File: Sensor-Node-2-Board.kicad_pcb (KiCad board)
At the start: 2 copper layers, 100 x 100 mm, 67 parts, among them J401 EBWA-02-B, J701 PS0519, J702 EBWA-02-B, Q101 BC549, Q401 Si4944DY, SW501 SW_HELP, U201 LM393, U601 Photon 2, U701 L7805

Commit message: feat: release
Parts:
- moved C701 12.6 mm to (203.0, 168.7)
- moved D702 12.6 mm to (192.5, 168.7)
- moved C101 12.6 mm to (260.0, 125.0)
- moved C102 12.6 mm to (232.5, 140.0)
- moved C103 12.6 mm to (248.8, 115.0)
- moved C201 12.6 mm to (250.0, 90.0)
- moved C202 12.6 mm to (231.3, 93.8)
- moved C301 12.6 mm to (218.7, 125.0)
- moved C401 12.6 mm to (180.0, 127.5)
- moved C402 12.6 mm to (185.0, 131.2)
- moved C501 12.6 mm to (181.2, 111.2)
- moved C502 12.6 mm to (205.0, 125.0)
- moved D101 12.6 mm to (252.5, 120.0)
- moved D401 12.6 mm to (180.0, 131.2)
- moved D501 12.6 mm to (175.0, 100.0)
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
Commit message: Update Outputs (release)
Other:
- board text added: "0.02mm"
- board text added: "0.035mm (1.00oz)"
- board text added: "1.49mm"
- board text added: "B.Mask"
- board text added: "B.Paste"
- board text added: "B.Silkscreen"
- board text added: "Copper"
- board text added: "Core"
- board text added: "Dielectric"
- board text added: "Direct Printing"
- board text added: "F.Mask"
- board text added: "F.Paste"
- board text added: "F.Silkscreen"
- board text added: "FR4_7628"
- board text added: "GBR"
- board text added: "Gerber"
- board text added: "L1 (Sig, PWR)"
- board text added: "L2 (Sig, GND)"
- board text added: "Layer"
- board text added: "Legend"
- board text added: "Material"
- board text added: "Note: external layer thicknesses are specified after plating"
- board text added: "Paste Mask"
- board text added: "Signal"
- board text added: "Solder Mask"
- board text added: "Solder Resist"
- board text added: "Thickness"
- board text added: "Total thickness: 1.6mm"
- board text added: "Type"

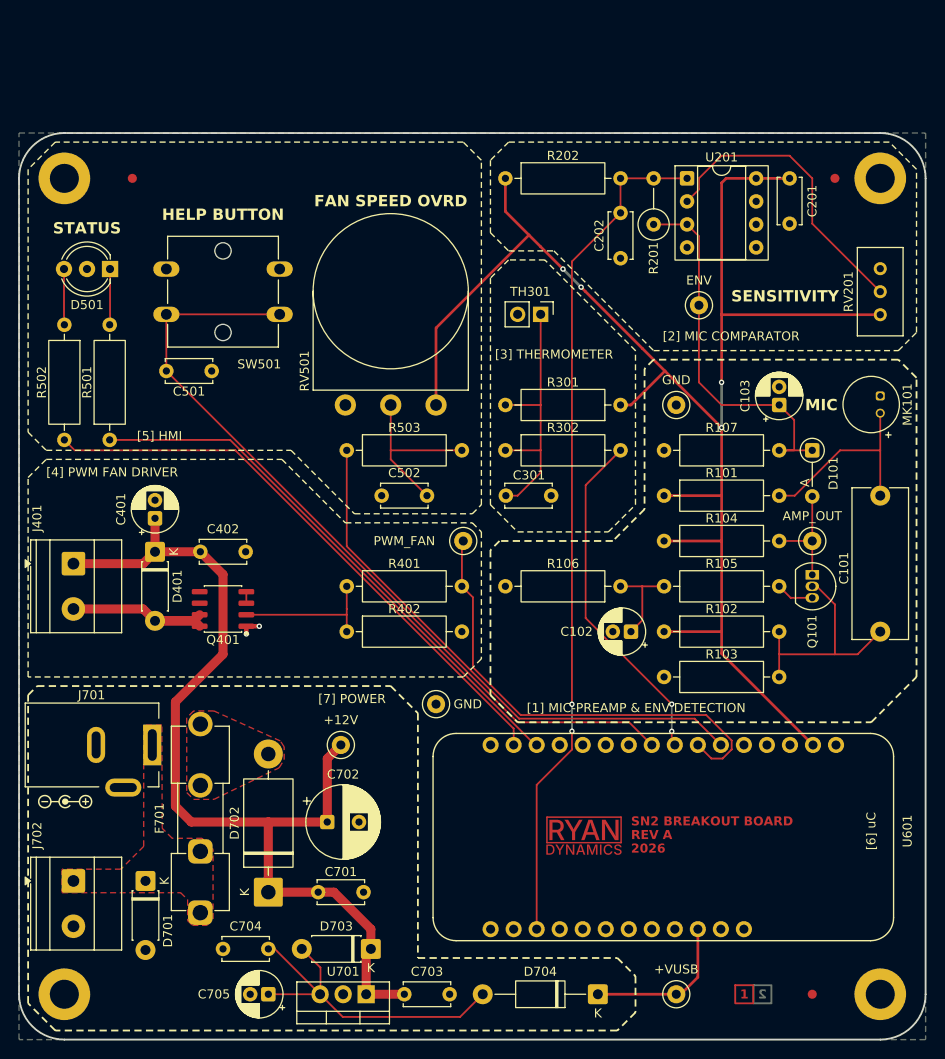
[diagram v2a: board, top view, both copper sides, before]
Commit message: fix: change status led wiring and improve 12V input protection
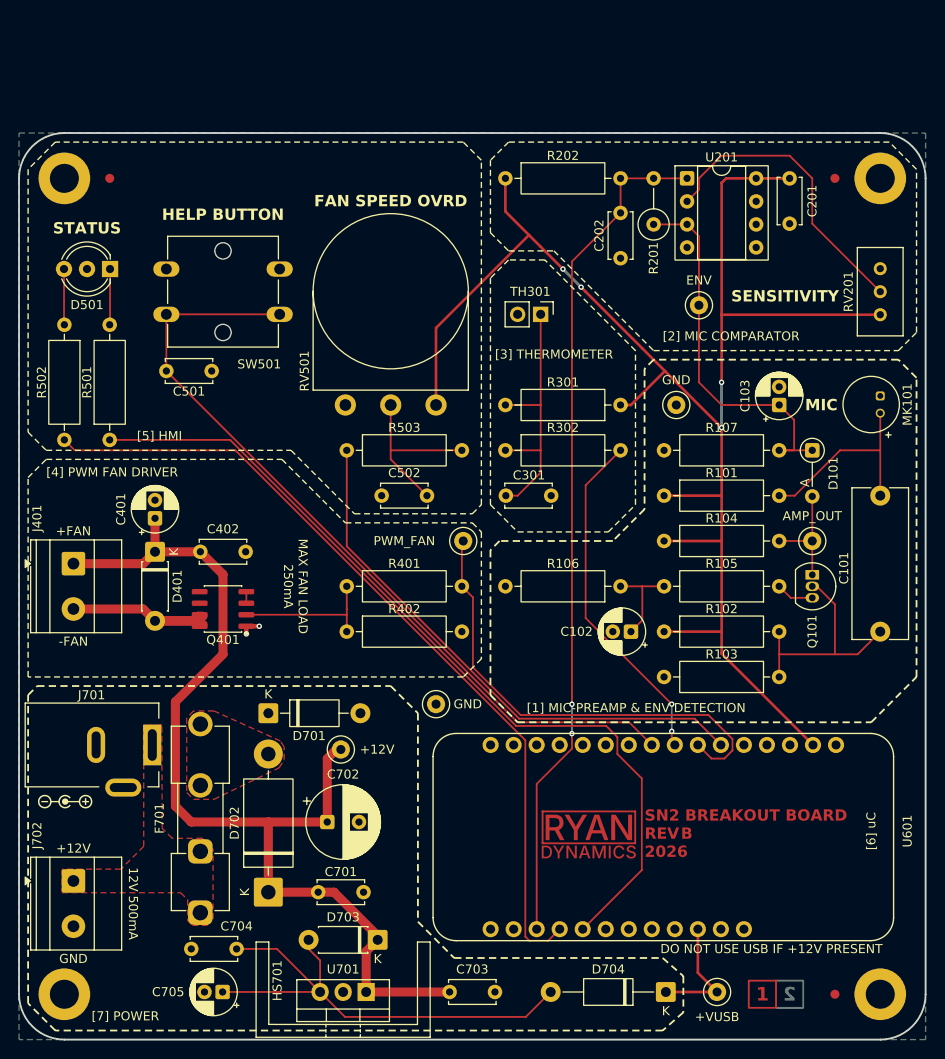
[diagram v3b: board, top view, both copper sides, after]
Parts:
- added HS701: Heatsink, RD-Heatsinks:Heatsink_6073B_19x9.5mm, F.Cu at (200.8, 184.6)
- D701: value P4KE16AC -> P4KE16; footprint Diode_THT:D_DO-41_SOD81_P7.62mm_Horizontal -> Diode_THT:D_DO-41_SOD81_P10.16mm_Horizontal
- F701: value 1A M205 -> 500mA M205
- ID901: footprint RD-Symbols-Silkscreen:STACKUP_ID_2L_SML -> RD-Symbols-Silkscreen:STACKUP_ID_2L
- moved D701 22.9 mm to (192.5, 149.0), turned to 0 degrees
- moved D704 7.50 mm to (236.3, 179.8)
- moved C705 5.05 mm to (187.5, 179.8)
- moved C703 5.01 mm to (217.5, 179.8)
- moved TP701 4.51 mm to (242.0, 179.8)
- moved C704 3.50 mm to (184.0, 175.0)
- moved FID901 2.50 mm to (175.0, 90.0)
- moved FID903 2.50 mm to (255.0, 180.0)
- moved ID901 2.50 mm to (248.5, 180.0)
- moved D703 1.25 mm to (204.6, 174.0)
- moved TP702 0.50 mm to (200.5, 153.0)
- moved U701 0.25 mm to (203.3, 179.8)
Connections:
- D701 pad 1: /SCHEMATIC/+12V_IN -> /SCHEMATIC/+12V_FUSED
- U601 pad 14: /SCHEMATIC/LED_RED -> unconnected-(U601-RX-Pad14)
- U601 pad 15: /SCHEMATIC/LED_GRN -> unconnected-(U601-TX-Pad15)
- U601 pad 20: unconnected-(U601-D3-Pad20) -> /SCHEMATIC/LED_GRN
- U601 pad 21: unconnected-(U601-D4-Pad21) -> /SCHEMATIC/LED_RED
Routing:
- net /SCHEMATIC/LED_RED: track 61.0 -> 94.6 mm
- net /SCHEMATIC/LED_GRN: track 64.6 -> 90.7 mm
- net /SCHEMATIC/+5V: track 39.4 -> 55.1 mm
- net +12V: track 108.5 -> 113.8 mm
- net +VUSB: track 17.1 -> 13.6 mm
- net /SCHEMATIC/FAN-: track 19.9 -> 20.5 mm
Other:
- board text added: "+12V"
- board text added: "+FAN"
- board text added: "-FAN"
- board text added: "12V 500mA"
- board text added: "B"
- board text added: "DO NOT USE USB IF +12V PRESENT"
- board text added: "GND"
- board text added: "MAX FAN LOAD 250mA"
- board text removed: "A"
